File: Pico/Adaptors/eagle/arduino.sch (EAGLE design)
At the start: 10 parts, among them J1 JST-2P-SMD-PW-3410050P1, U3 MAX1551

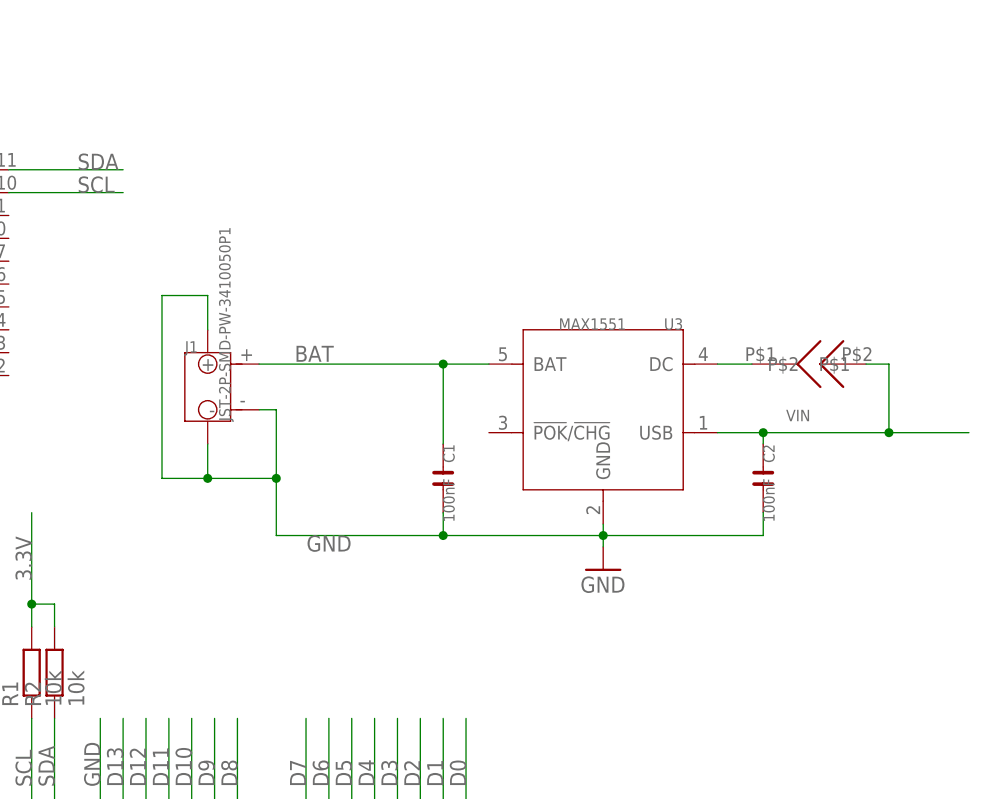
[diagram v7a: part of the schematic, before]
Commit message: Added battery charger pads to proto headers
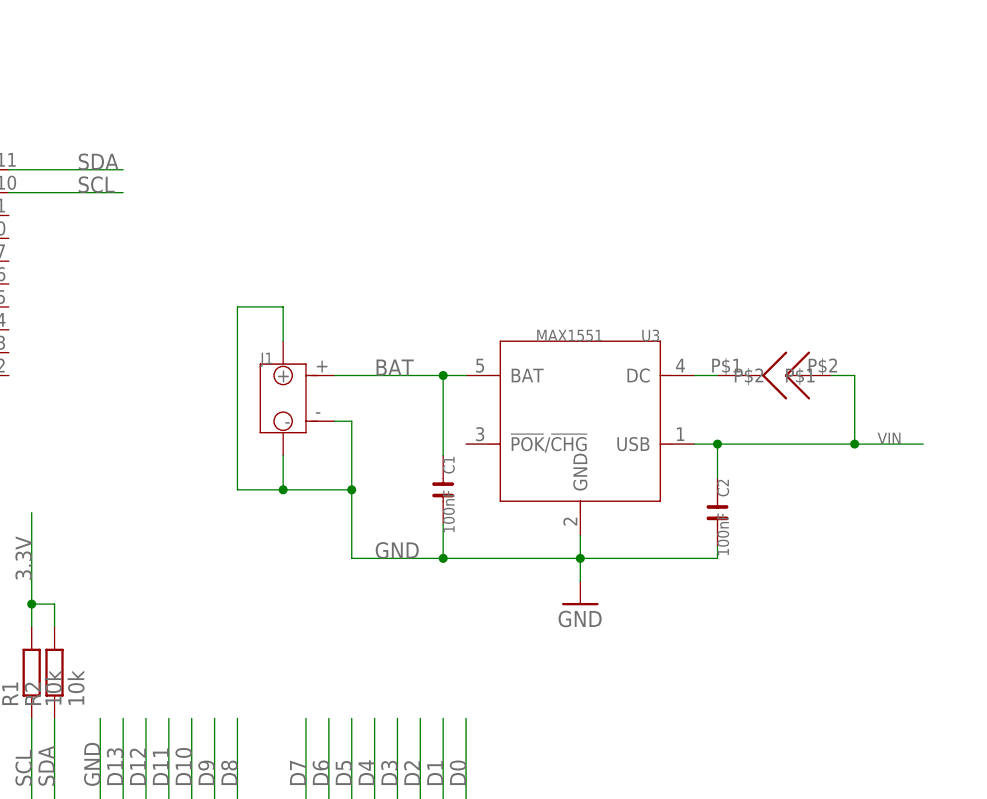
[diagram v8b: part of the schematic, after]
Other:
- moved on the sheet: C1, C2, J1, U3
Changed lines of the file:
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@@
 <part name="R1" library="rcl" deviceset="R-EU_" device="R0805" value="10k"/>
 <part name="R2" library="rcl" deviceset="R-EU_" device="R0805" value="10k"/>
-<part name="J1" library="OPL Eagle Library" deviceset="JST-2P-SMD-PW" device="-3410050P1"/>
+<part name="J1" library="OPL Eagle Library" deviceset="JST-2P-SMD-PW" device="-3410050P1" value=""/>
 <part name="U3" library="template" deviceset="MAX1551" device="" value="MAX1551"/>
 <part name="GND26" library="supply1" deviceset="GND" device=""/>
@@
 <instance part="R1" gate="G$1" x="60.96" y="78.74" rot="R90"/>
 <instance part="R2" gate="G$1" x="63.5" y="78.74" rot="R90"/>
-<instance part="J1" gate="J" x="80.518" y="110.49"/>
-<instance part="U3" gate="G$1" x="124.46" y="107.95" rot="MR0"/>
-<instance part="GND26" gate="1" x="124.46" y="90.17"/>
-<instance part="C2" gate="C" x="142.24" y="100.33" rot="R270"/>
-<instance part="C1" gate="C" x="106.68" y="100.33" rot="R270"/>
-<instance part="U$4" gate="G$1" x="148.59" y="113.03"/>
+<instance part="J1" gate="J" x="88.9" y="109.22"/>
+<instance part="U3" gate="G$1" x="121.92" y="106.68" rot="MR0"/>
+<instance part="GND26" gate="1" x="121.92" y="86.36"/>
+<instance part="C2" gate="C" x="137.16" y="96.52" rot="R270"/>
+<instance part="C1" gate="C" x="106.68" y="99.06" rot="R270"/>
+<instance part="U$4" gate="G$1" x="144.78" y="111.76"/>
 </instances>
 <busses>
@@
 <pinref part="U3" gate="G$1" pin="GND"/>
 <pinref part="GND26" gate="1" pin="GND"/>
-<wire x1="124.46" y1="92.71" x2="124.46" y2="93.98" width="0.1524" layer="91"/>
+<wire x1="121.92" y1="88.9" x2="121.92" y2="91.44" width="0.1524" layer="91"/>
 <pinref part="C1" gate="C" pin="2"/>
-<wire x1="124.46" y1="93.98" x2="124.46" y2="95.25" width="0.1524" layer="91"/>
-<wire x1="106.68" y1="96.52" x2="106.68" y2="93.98" width="0.1524" layer="91"/>
-<wire x1="106.68" y1="93.98" x2="124.46" y2="93.98" width="0.1524" layer="91"/>
-<junction x="124.46" y="93.98"/>
+<wire x1="121.92" y1="91.44" x2="121.92" y2="93.98" width="0.1524" layer="91"/>
+<wire x1="106.68" y1="95.25" x2="106.68" y2="91.44" width="0.1524" layer="91"/>
+<wire x1="106.68" y1="91.44" x2="121.92" y2="91.44" width="0.1524" layer="91"/>
+<junction x="121.92" y="91.44"/>
 <pinref part="C2" gate="C" pin="2"/>
-<wire x1="124.46" y1="93.98" x2="142.24" y2="93.98" width="0.1524" layer="91"/>
-<wire x1="142.24" y1="93.98" x2="142.24" y2="96.52" width="0.1524" layer="91"/>
+<wire x1="121.92" y1="91.44" x2="137.16" y2="91.44" width="0.1524" layer="91"/>
+<wire x1="137.16" y1="91.44" x2="137.16" y2="92.71" width="0.1524" layer="91"/>
 <pinref part="J1" gate="J" pin="-"/>
-<wire x1="86.233" y1="107.95" x2="88.138" y2="107.95" width="0.1524" layer="91"/>
-<wire x1="88.138" y1="100.33" x2="88.138" y2="93.98" width="0.1524" layer="91"/>
-<wire x1="88.138" y1="107.95" x2="88.138" y2="100.33" width="0.1524" layer="91"/>
-<wire x1="88.138" y1="100.33" x2="80.518" y2="100.33" width="0.1524" layer="91"/>
-<wire x1="80.518" y1="100.33" x2="75.438" y2="100.33" width="0.1524" layer="91"/>
-<wire x1="75.438" y1="100.33" x2="75.438" y2="120.65" width="0.1524" layer="91"/>
-<wire x1="75.438" y1="120.65" x2="80.518" y2="120.65" width="0.1524" layer="91"/>
-<wire x1="80.518" y1="120.65" x2="80.518" y2="116.84" width="0.1524" layer="91"/>
-<wire x1="80.518" y1="100.33" x2="80.518" y2="104.14" width="0.1524" layer="91"/>
+<wire x1="94.615" y1="106.68" x2="96.52" y2="106.68" width="0.1524" layer="91"/>
+<wire x1="96.52" y1="99.06" x2="96.52" y2="91.44" width="0.1524" layer="91"/>
+<wire x1="96.52" y1="106.68" x2="96.52" y2="99.06" width="0.1524" layer="91"/>
+<wire x1="96.52" y1="99.06" x2="88.9" y2="99.06" width="0.1524" layer="91"/>
+<wire x1="88.9" y1="99.06" x2="83.82" y2="99.06" width="0.1524" layer="91"/>
+<wire x1="83.82" y1="99.06" x2="83.82" y2="119.38" width="0.1524" layer="91"/>
+<wire x1="83.82" y1="119.38" x2="88.9" y2="119.38" width="0.1524" layer="91"/>
+<wire x1="88.9" y1="119.38" x2="88.9" y2="115.57" width="0.1524" layer="91"/>
+<wire x1="88.9" y1="99.06" x2="88.9" y2="102.87" width="0.1524" layer="91"/>
 <pinref part="J1" gate="J" pin="3"/>
 <pinref part="J1" gate="J" pin="4"/>
-<label x="96.52" y="93.98" size="1.778" layer="95" rot="R180"/>
-<wire x1="106.68" y1="93.98" x2="88.138" y2="93.98" width="0.1524" layer="91"/>
-<junction x="80.518" y="100.33"/>
-<junction x="88.138" y="100.33"/>
-<junction x="106.68" y="93.98"/>
+<label x="99.06" y="91.44" size="1.778" layer="95"/>
+<wire x1="106.68" y1="91.44" x2="96.52" y2="91.44" width="0.1524" layer="91"/>
+<junction x="88.9" y="99.06"/>
+<junction x="96.52" y="99.06"/>
+<junction x="106.68" y="91.44"/>
 </segment>
 </net>
@@
 <segment>
 <pinref part="U3" gate="G$1" pin="USB"/>
-<wire x1="137.16" y1="105.41" x2="142.24" y2="105.41" width="0.1524" layer="91"/>
-<label x="144.78" y="106.68" size="1.27" layer="95" ratio="10"/>
+<wire x1="134.62" y1="104.14" x2="137.16" y2="104.14" width="0.1524" layer="91"/>
+<label x="154.94" y="104.14" size="1.27" layer="95" ratio="10"/>
 <pinref part="C2" gate="C" pin="1"/>
-<wire x1="142.24" y1="104.14" x2="142.24" y2="105.41" width="0.1524" layer="91"/>
-<junction x="142.24" y="105.41"/>
-<wire x1="142.24" y1="105.41" x2="156.21" y2="105.41" width="0.1524" layer="91"/>
+<wire x1="137.16" y1="100.33" x2="137.16" y2="104.14" width="0.1524" layer="91"/>
+<junction x="137.16" y="104.14"/>
+<wire x1="137.16" y1="104.14" x2="152.4" y2="104.14" width="0.1524" layer="91"/>
 <pinref part="U$4" gate="G$1" pin="P$2"/>
-<wire x1="156.21" y1="105.41" x2="165.1" y2="105.41" width="0.1524" layer="91"/>
-<wire x1="153.67" y1="113.03" x2="156.21" y2="113.03" width="0.1524" layer="91"/>
-<wire x1="156.21" y1="113.03" x2="156.21" y2="105.41" width="0.1524" layer="91"/>
-<junction x="156.21" y="105.41"/>
-<wire x1="156.21" y1="105.41" x2="156.21" y2="105.156" width="0.1524" layer="91"/>
+<wire x1="152.4" y1="104.14" x2="160.02" y2="104.14" width="0.1524" layer="91"/>
+<wire x1="149.86" y1="111.76" x2="152.4" y2="111.76" width="0.1524" layer="91"/>
+<wire x1="152.4" y1="111.76" x2="152.4" y2="104.14" width="0.1524" layer="91"/>
+<junction x="152.4" y="104.14"/>
 </segment>
 </net>
@@
 <pinref part="U3" gate="G$1" pin="BAT"/>
 <pinref part="C1" gate="C" pin="1"/>
-<wire x1="86.233" y1="113.03" x2="106.68" y2="113.03" width="0.1524" layer="91"/>
-<wire x1="106.68" y1="113.03" x2="111.76" y2="113.03" width="0.1524" layer="91"/>
-<wire x1="106.68" y1="104.14" x2="106.68" y2="113.03" width="0.1524" layer="91"/>
-<junction x="106.68" y="113.03"/>
+<wire x1="94.615" y1="111.76" x2="106.68" y2="111.76" width="0.1524" layer="91"/>
+<wire x1="106.68" y1="111.76" x2="109.22" y2="111.76" width="0.1524" layer="91"/>
+<wire x1="106.68" y1="102.87" x2="106.68" y2="111.76" width="0.1524" layer="91"/>
+<junction x="106.68" y="111.76"/>
 <pinref part="J1" gate="J" pin="+"/>
-<label x="90.17" y="113.284" size="1.778" layer="95"/>
+<label x="99.06" y="111.76" size="1.778" layer="95"/>
 </segment>
 </net>
@@
 <pinref part="U3" gate="G$1" pin="DC"/>
 <pinref part="U$4" gate="G$1" pin="P$1"/>
-<wire x1="140.97" y1="113.03" x2="137.16" y2="113.03" width="0.1524" layer="91"/>
-</segment>
-</net>
+<wire x1="137.16" y1="111.76" x2="134.62" y2="111.76" width="0.1524" layer="91"/>
+</segment>
+</net>
